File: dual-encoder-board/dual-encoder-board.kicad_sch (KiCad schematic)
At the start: 7 parts, among them U1 EC11EBB24C03

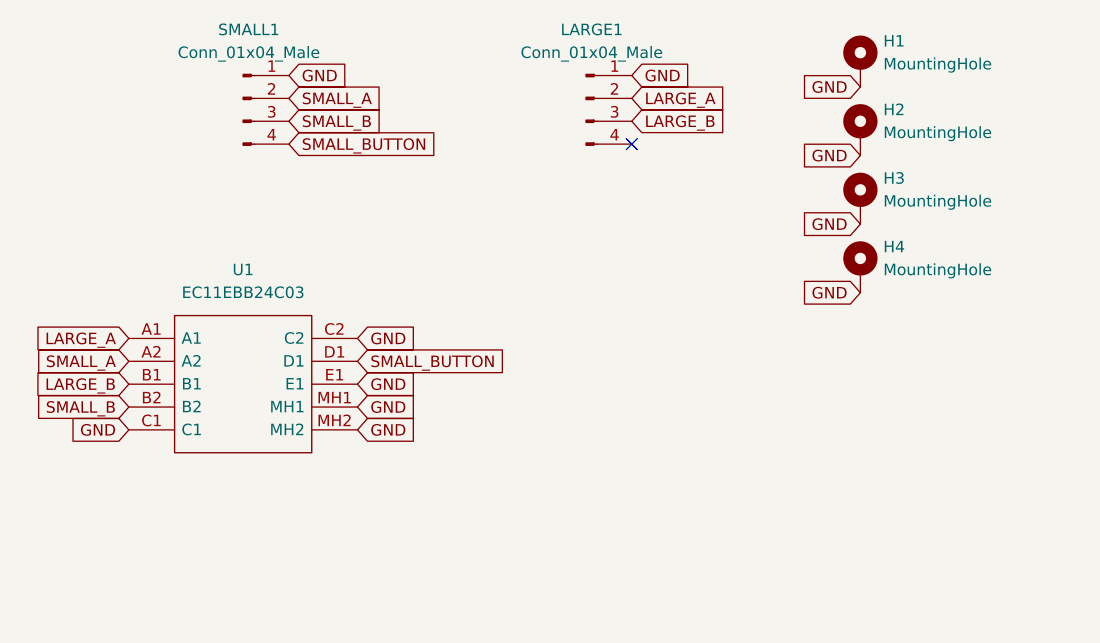
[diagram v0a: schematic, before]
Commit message: sync the jst connector type between schema and pcb
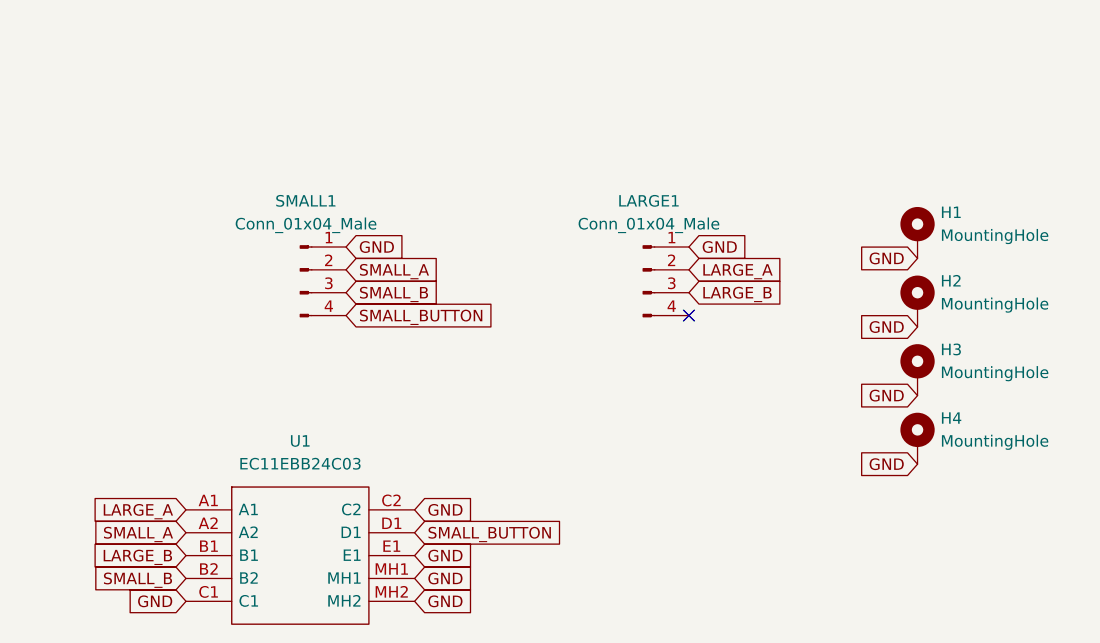
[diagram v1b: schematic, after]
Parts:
- LARGE1, SMALL1: footprint Connector_JST:JST_XH_B4B-XH-AM_1x04_P2.50mm_Vertical -> Connector_JST:JST_XH_B4B-XH-A_1x04_P2.50mm_Vertical
- U1: footprint EC11EBB24C03 -> KiCad:EC11EBB24C03
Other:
- moved on the sheet: H1, H2, H3, H4, LARGE1, SMALL1, U1

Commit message: updated button pin to outer encoder connector so it works for single encoders also
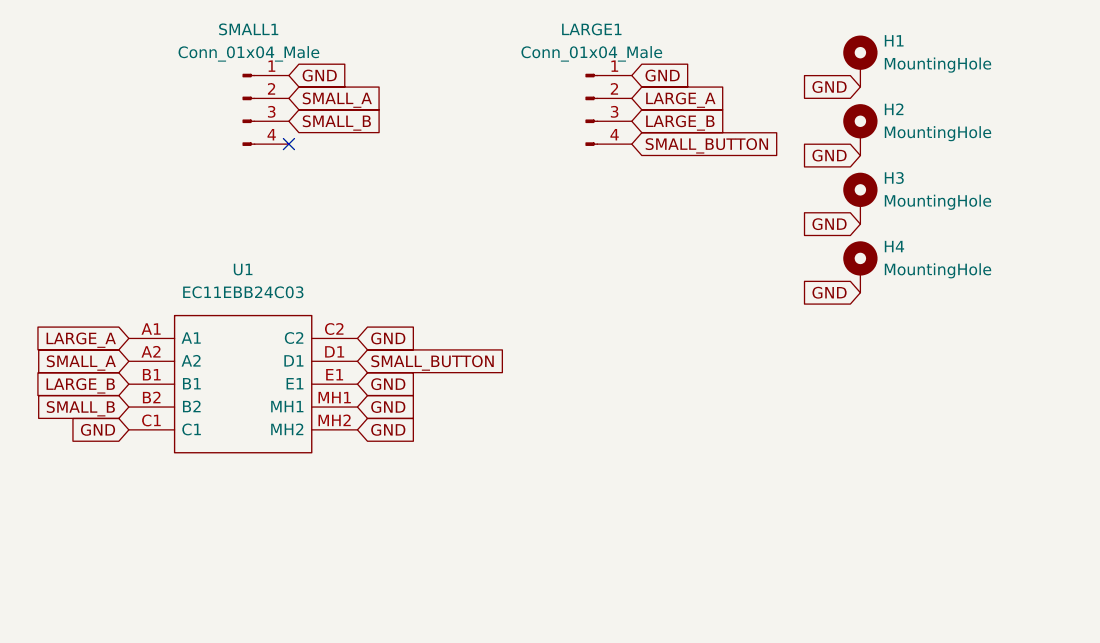
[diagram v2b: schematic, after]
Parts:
- U1: footprint KiCad:EC11EBB24C03 -> EC11EBB24C03
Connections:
- net SMALL_BUTTON: now also LARGE1.4 (Pin_4); no longer SMALL1.4 (Pin_4)
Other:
- moved on the sheet: H1, H2, H3, H4, LARGE1, SMALL1, U1

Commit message: fixed net names
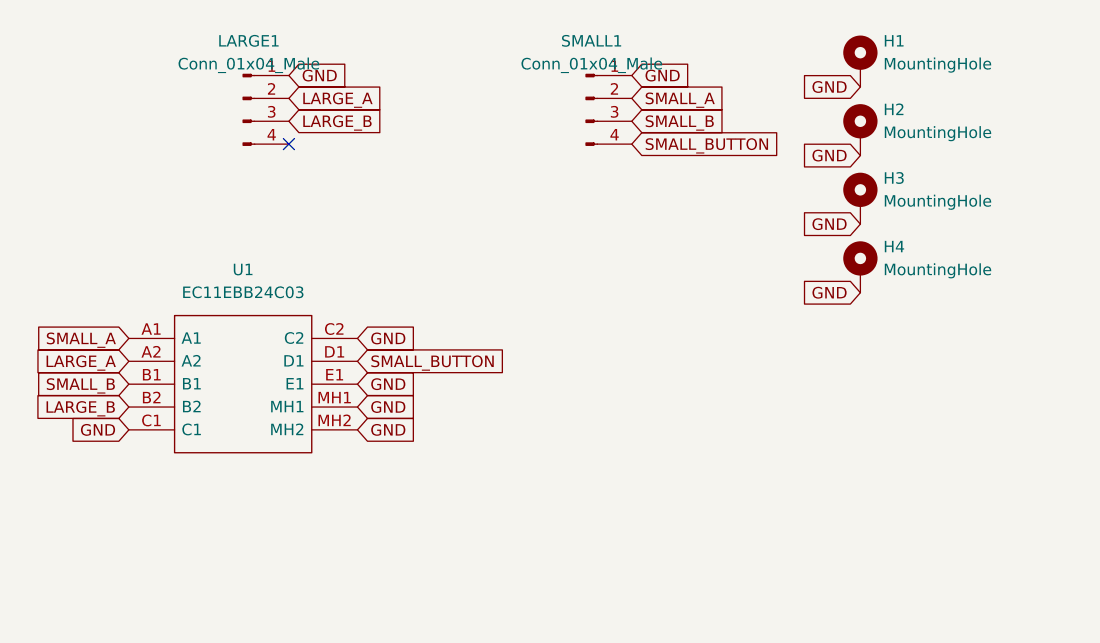
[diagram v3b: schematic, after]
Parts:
- U1: footprint EC11EBB24C03 -> MobiFlight:EC11EBB24C03
- renumbered SMALL1 to LARGE1, LARGE1 to SMALL1
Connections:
- net LARGE_A: now also LARGE1.2 (Pin_2), U1.A2; no longer SMALL1.2 (Pin_2), U1.A1
- net LARGE_B: now also LARGE1.3 (Pin_3), U1.B2; no longer SMALL1.3 (Pin_3), U1.B1
- net SMALL_A: now also SMALL1.2 (Pin_2), U1.A1; no longer LARGE1.2 (Pin_2), U1.A2
- net SMALL_B: now also SMALL1.3 (Pin_3), U1.B1; no longer LARGE1.3 (Pin_3), U1.B2
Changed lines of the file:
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@@
-    )
-  )
-  (global_label "LARGE_B" (shape input) (at 92.71 29.21 0) (fields_autoplaced)
-    (effects (font (size 1.27 1.27)) (justify left))
-    (property "Intersheetrefs" "${INTERSHEET_REFS}" (at 103.1664 29.2894 0)
-      (effects (font (size 1.27 1.27)) (justify left) hide)
     )
   )
@@
     )
   )
+  (global_label "LARGE_A" (shape input) (at 54.61 26.67 0) (fields_autoplaced)
+    (effects (font (size 1.27 1.27)) (justify left))
+    (property "Intersheetrefs" "${INTERSHEET_REFS}" (at 64.885 26.7494 0)
+      (effects (font (size 1.27 1.27)) (justify left) hide)
+    )
+  )
   (global_label "GND" (shape input) (at 118.11 25.4 180) (fields_autoplaced)
     (effects (font (size 1.27 1.27)) (justify right))
@@
     )
   )
-  (global_label "SMALL_A" (shape input) (at 54.61 26.67 0) (fields_autoplaced)
-    (effects (font (size 1.27 1.27)) (justify left))
-    (property "Intersheetrefs" "${INTERSHEET_REFS}" (at 64.885 26.5906 0)
+  (global_label "SMALL_A" (shape input) (at 92.71 26.67 0) (fields_autoplaced)
+    (effects (font (size 1.27 1.27)) (justify left))
+    (property "Intersheetrefs" "${INTERSHEET_REFS}" (at 102.985 26.5906 0)
+      (effects (font (size 1.27 1.27)) (justify left) hide)
+    )
+  )
+  (global_label "LARGE_B" (shape input) (at 54.61 29.21 0) (fields_autoplaced)
+    (effects (font (size 1.27 1.27)) (justify left))
+    (property "Intersheetrefs" "${INTERSHEET_REFS}" (at 65.0664 29.2894 0)
       (effects (font (size 1.27 1.27)) (justify left) hide)
     )
@@
     )
   )
-  (global_label "LARGE_A" (shape input) (at 92.71 26.67 0) (fields_autoplaced)
-    (effects (font (size 1.27 1.27)) (justify left))
-    (property "Intersheetrefs" "${INTERSHEET_REFS}" (at 102.985 26.7494 0)
-      (effects (font (size 1.27 1.27)) (justify left) hide)
-    )
-  )
-  (global_label "SMALL_B" (shape input) (at 36.83 60.96 180) (fields_autoplaced)
+  (global_label "SMALL_B" (shape input) (at 92.71 29.21 0) (fields_autoplaced)
+    (effects (font (size 1.27 1.27)) (justify left))
+    (property "Intersheetrefs" "${INTERSHEET_REFS}" (at 103.1664 29.1306 0)
+      (effects (font (size 1.27 1.27)) (justify left) hide)
+    )
+  )
+  (global_label "SMALL_B" (shape input) (at 36.83 58.42 180) (fields_autoplaced)
+    (effects (font (size 1.27 1.27)) (justify right))
+    (property "Intersheetrefs" "${INTERSHEET_REFS}" (at 26.3736 58.4994 0)
+      (effects (font (size 1.27 1.27)) (justify right) hide)
+    )
+  )
+  (global_label "GND" (shape input) (at 62.23 53.34 0) (fields_autoplaced)
+    (effects (font (size 1.27 1.27)) (justify left))
+    (property "Intersheetrefs" "${INTERSHEET_REFS}" (at 68.5136 53.2606 0)
+      (effects (font (size 1.27 1.27)) (justify left) hide)
+    )
+  )
+  (global_label "GND" (shape input) (at 118.11 33.02 180) (fields_autoplaced)
+    (effects (font (size 1.27 1.27)) (justify right))
+    (property "Intersheetrefs" "${INTERSHEET_REFS}" (at 111.8264 33.0994 0)
+      (effects (font (size 1.27 1.27)) (justify right) hide)
+    )
+  )
+  (global_label "SMALL_A" (shape input) (at 36.83 53.34 180) (fields_autoplaced)
+    (effects (font (size 1.27 1.27)) (justify right))
+    (property "Intersheetrefs" "${INTERSHEET_REFS}" (at 26.555 53.4194 0)
+      (effects (font (size 1.27 1.27)) (justify right) hide)
+    )
+  )
+  (global_label "LARGE_A" (shape input) (at 36.83 55.88 180) (fields_autoplaced)
+    (effects (font (size 1.27 1.27)) (justify right))
+    (property "Intersheetrefs" "${INTERSHEET_REFS}" (at 26.555 55.8006 0)
+      (effects (font (size 1.27 1.27)) (justify right) hide)
+    )
+  )
+  (global_label "GND" (shape input) (at 62.23 58.42 0) (fields_autoplaced)
+    (effects (font (size 1.27 1.27)) (justify left))
+    (property "Intersheetrefs" "${INTERSHEET_REFS}" (at 68.5136 58.3406 0)
+      (effects (font (size 1.27 1.27)) (justify left) hide)
+    )
+  )
+  (global_label "LARGE_B" (shape input) (at 36.83 60.96 180) (fields_autoplaced)
     (effects (font (size 1.27 1.27)) (justify right))
     (property "Intersheetrefs" "${INTERSHEET_REFS}" (at 26.3736 60.8806 0)
@@
     )
   )
-  (global_label "GND" (shape input) (at 62.23 53.34 0) (fields_autoplaced)
-    (effects (font (size 1.27 1.27)) (justify left))
-    (property "Intersheetrefs" "${INTERSHEET_REFS}" (at 68.5136 53.2606 0)
-      (effects (font (size 1.27 1.27)) (justify left) hide)
-    )
-  )
-  (global_label "GND" (shape input) (at 118.11 33.02 180) (fields_autoplaced)
-    (effects (font (size 1.27 1.27)) (justify right))
-    (property "Intersheetrefs" "${INTERSHEET_REFS}" (at 111.8264 33.0994 0)
-      (effects (font (size 1.27 1.27)) (justify right) hide)
-    )
-  )
-  (global_label "SMALL_A" (shape input) (at 36.83 55.88 180) (fields_autoplaced)
-    (effects (font (size 1.27 1.27)) (justify right))
-    (property "Intersheetrefs" "${INTERSHEET_REFS}" (at 26.555 55.8006 0)
-      (effects (font (size 1.27 1.27)) (justify right) hide)
-    )
-  )
-  (global_label "LARGE_A" (shape input) (at 36.83 53.34 180) (fields_autoplaced)
-    (effects (font (size 1.27 1.27)) (justify right))
-    (property "Intersheetrefs" "${INTERSHEET_REFS}" (at 26.555 53.4194 0)
-      (effects (font (size 1.27 1.27)) (justify right) hide)
-    )
-  )
-  (global_label "GND" (shape input) (at 62.23 58.42 0) (fields_autoplaced)
-    (effects (font (size 1.27 1.27)) (justify left))
-    (property "Intersheetrefs" "${INTERSHEET_REFS}" (at 68.5136 58.3406 0)
-      (effects (font (size 1.27 1.27)) (justify left) hide)
-    )
-  )
-  (global_label "LARGE_B" (shape input) (at 36.83 58.42 180) (fields_autoplaced)
-    (effects (font (size 1.27 1.27)) (justify right))
-    (property "Intersheetrefs" "${INTERSHEET_REFS}" (at 26.3736 58.4994 0)
-      (effects (font (size 1.27 1.27)) (justify right) hide)
-    )
-  )
   (global_label "GND" (shape input) (at 118.11 40.64 180) (fields_autoplaced)
     (effects (font (size 1.27 1.27)) (justify right))
@@
     )
   )
-  (global_label "SMALL_B" (shape input) (at 54.61 29.21 0) (fields_autoplaced)
-    (effects (font (size 1.27 1.27)) (justify left))
-    (property "Intersheetrefs" "${INTERSHEET_REFS}" (at 65.0664 29.1306 0)
-      (effects (font (size 1.27 1.27)) (justify left) hide)
-    )
-  )
   (symbol (lib_id "Mechanical:MountingHole_Pad") (at 118.11 38.1 0) (unit 1)
     (in_bom yes) (on_board yes) (dnp no) (fields_autoplaced)
@@
   (symbol (lib_id "Connector:Conn_01x04_Male") (at 49.53 26.67 0) (unit 1)
     (in_bom yes) (on_board yes) (dnp no) (fields_autoplaced)
-    (property "Reference" "SMALL1" (at 50.165 19.05 0)
-      (effects (font (size 1.27 1.27)))
-    )
-    (property "Value" "Conn_01x04_Male" (at 50.165 21.59 0)
+    (property "Reference" "LARGE1" (at 50.165 20.32 0)
+      (effects (font (size 1.27 1.27)))
+    )
+    (property "Value" "Conn_01x04_Male" (at 50.165 22.86 0)
       (effects (font (size 1.27 1.27)))
     )
@@
       (project "dual-encoder-board"
         (path "/d04844d1-8779-4547-9d30-86688eb51b8d"
-          (reference "SMALL1") (unit 1)
+          (reference "LARGE1") (unit 1)
         )
       )
@@
   (symbol (lib_id "Connector:Conn_01x04_Male") (at 87.63 26.67 0) (unit 1)
     (in_bom yes) (on_board yes) (dnp no) (fields_autoplaced)
-    (property "Reference" "LARGE1" (at 88.265 19.05 0)
-      (effects (font (size 1.27 1.27)))
-    )
-    (property "Value" "Conn_01x04_Male" (at 88.265 21.59 0)
+    (property "Reference" "SMALL1" (at 88.265 20.32 0)
+      (effects (font (size 1.27 1.27)))
+    )
+    (property "Value" "Conn_01x04_Male" (at 88.265 22.86 0)
       (effects (font (size 1.27 1.27)))
     )
@@
       (project "dual-encoder-board"
         (path "/d04844d1-8779-4547-9d30-86688eb51b8d"
-          (reference "LARGE1") (unit 1)
+          (reference "SMALL1") (unit 1)
         )
       )
@@
       (effects (font (size 1.27 1.27)))
     )
-    (property "Footprint" "EC11EBB24C03" (at 58.42 50.8 0)
-      (effects (font (size 1.27 1.27)) (justify left) hide)
-    )
+    (property "Footprint" "MobiFlight:EC11EBB24C03" (at 58.42 50.8 0)
+      (effects (font (size 1.27 1.27)) (justify left) hide)
+    )

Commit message: Update all boards to KiCad 9.0 (#44)
* update dimmer board to KiCad version 9

* update dual encoder board to KiCad version 9

* update input shifter board, start numbering with zero instead one

* update MAX7219 breakout board to KiCad version 9

* add 3 pol JST connector

* updatge template to KiCad version 9

* update potentiometer board to KiCad version 9, use JST connector from MF lib

* update 6pin JST connector

* update prototyping board to KiCad version 9

* update symbols on dimmer board, fixed DRC

* update symbols from MAX7219 breakout board

* add Screw Terminalblocks to footprint lib and 3D models

* use screw terminals from MF lib

* fixed outline of Potentiometer board

* fixed missing IDC footprints error

* add MAX7219 symbol

* use MAX7219 symbol from MF lib

* add Mega2560mini symbol and footprint to MF library

* use Mega2560mini symbol and footprint from MF library

* add used Dual Encoder symbol and footprint to MF lib

* use footprint and symbol for Dual Encoder from MF lib
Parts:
- U1: footprint MobiFlight:EC11EBB24C03 -> MobiFlight:EC11EBB24C03_oval; symbol EC11EBB24C03:EC11EBB24C03 -> mobiflight-library:EC11EBB24C03
